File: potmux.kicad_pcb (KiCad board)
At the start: 2 copper layers, 22.9 x 26.7 mm, 8 parts, among them P1 SOCKET_LEFT, P2 KEYMAN64, P3 SOCKET_RIGHT, U1 4052, U2 4052

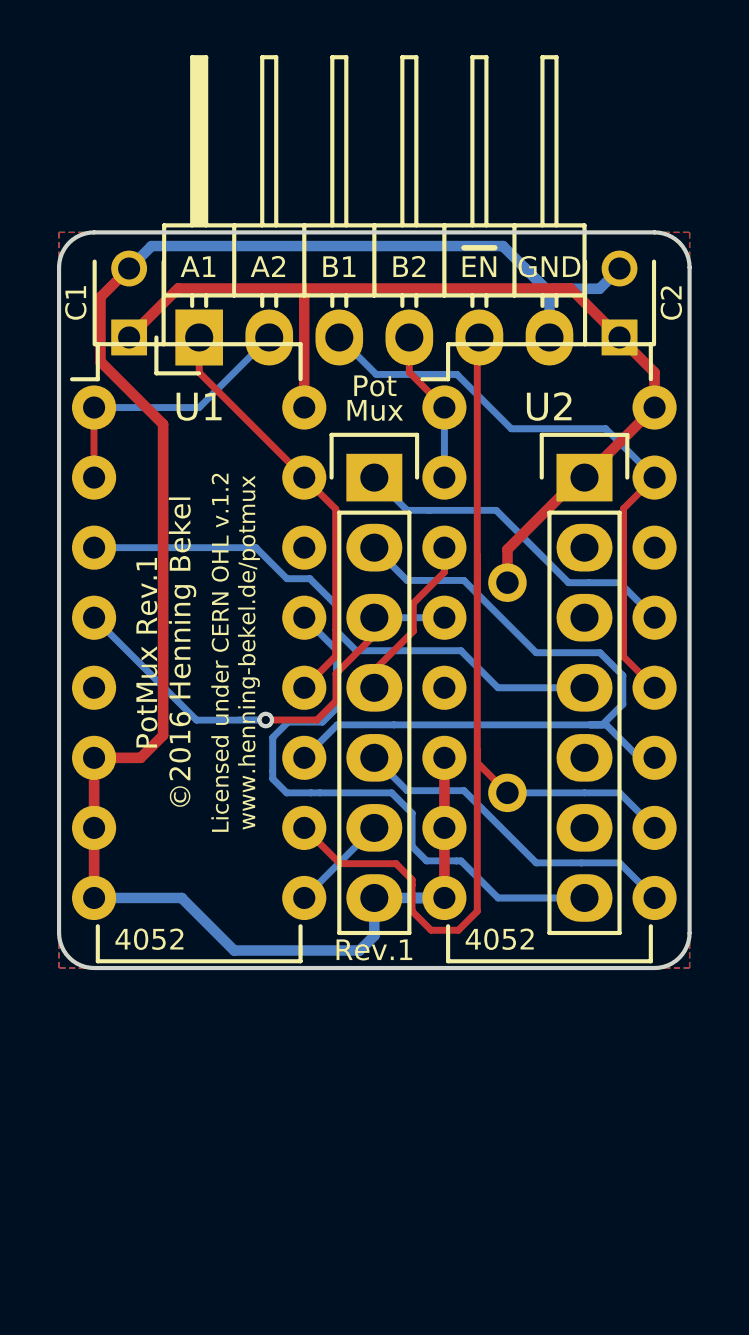
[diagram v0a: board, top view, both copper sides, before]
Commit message: Revision 2, updated gerber files for production
This revision moves the pin header to the bottom.
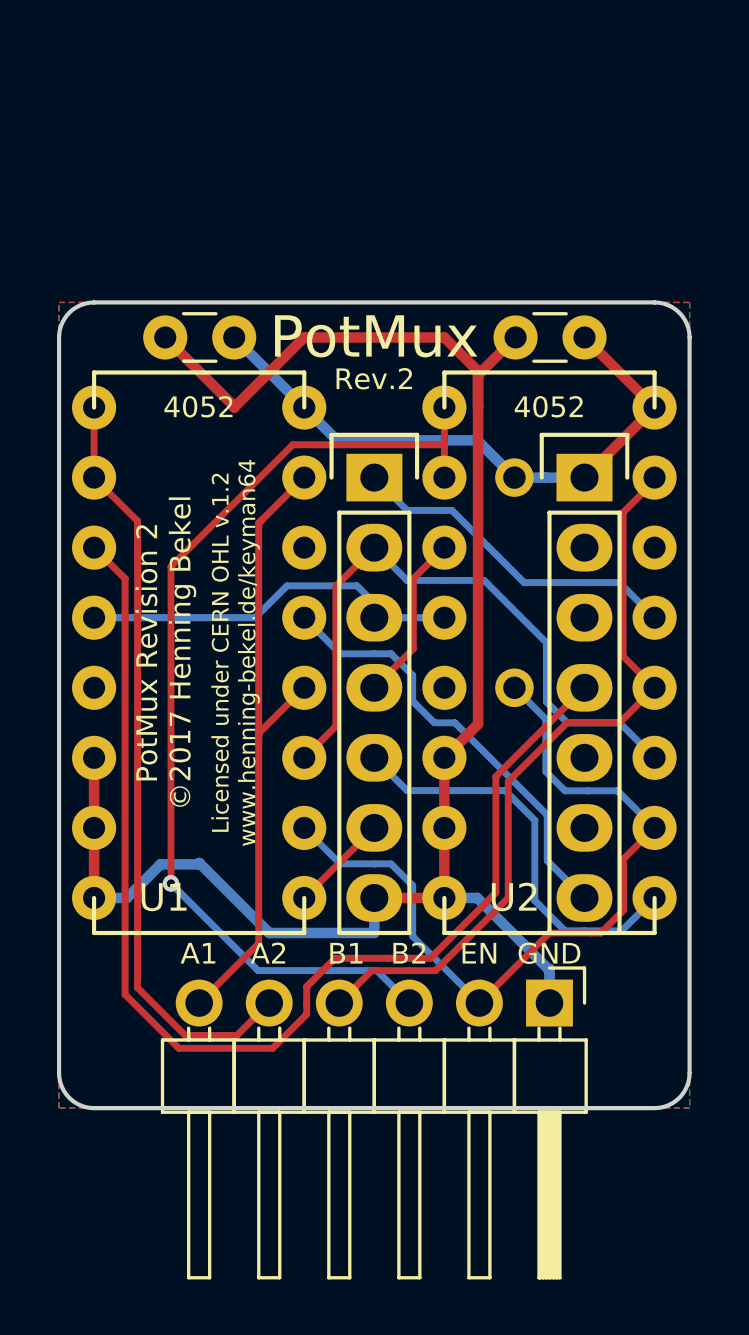
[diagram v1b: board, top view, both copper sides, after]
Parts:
- removed P2: KEYMAN64, Pin_Headers:Pin_Header_Angled_1x06
- added P4: KEYMAN64, Pin_Headers:Pin_Header_Angled_1x06_Pitch2.54mm, F.Cu at (148.6, 115.6)
- C1, C2: footprint Capacitors_ThroughHole:C_Disc_D3_P2.5 -> Capacitors_ThroughHole:C_Disc_D3.0mm_W1.6mm_P2.50mm
- U1, U2: footprint Housings_DIP:DIP-16_W7.62mm -> custom:DIP-16_W7.62mm
- moved C2 16.5 mm to (149.9, 91.4), turned to 180 degrees
- moved C1 14.0 mm to (137.2, 91.4), turned to 180 degrees
- moved R1 3.82 mm to (147.3, 100.3)
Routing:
- net /B2: track 5.61 -> 36.2 mm, vias 0 -> 1
- net /POTAY: track 20.4 -> 42.6 mm
- net /A2: track 9.94 -> 27.7 mm
- net VCC: track 36.0 -> 22.0 mm
- net /~EN: track 39.1 -> 28.4 mm
- net /A1: track 16.5 -> 23.5 mm
- net GND: track 70.2 -> 64.1 mm
- net /POTAX: track 21.8 -> 15.9 mm
- net /B1: track 22.1 -> 27.7 mm
- net /POTX: track 27.2 -> 23.2 mm
- net /POTY: track 16.7 -> 14.0 mm, vias 1 -> 0
- net /PA7: track 12.3 -> 15.0 mm
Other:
- board size 22.9 x 26.7 mm -> 22.9 x 29.2 mm
- board text added: "Licensed under CERN OHL v.1.2 www.henning-bekel.de/keyman64"
- board text added: "PotMux"
- board text added: "PotMux Revision 2 ©2017 Henning Bekel"
- board text added: "Rev.2"
- board text removed: "C1"
- board text removed: "C2"
- board text removed: "Licensed under CERN OHL v.1.2 www.henning-bekel.de/potmux"
- board text removed: "Mux"
- board text removed: "Pot"
- board text removed: "PotMux Rev.1 ©2016 Henning Bekel"
- board text removed: "Rev.1"
